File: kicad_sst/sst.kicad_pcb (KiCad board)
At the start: 2 copper layers, 75 x 75 mm, 35 parts

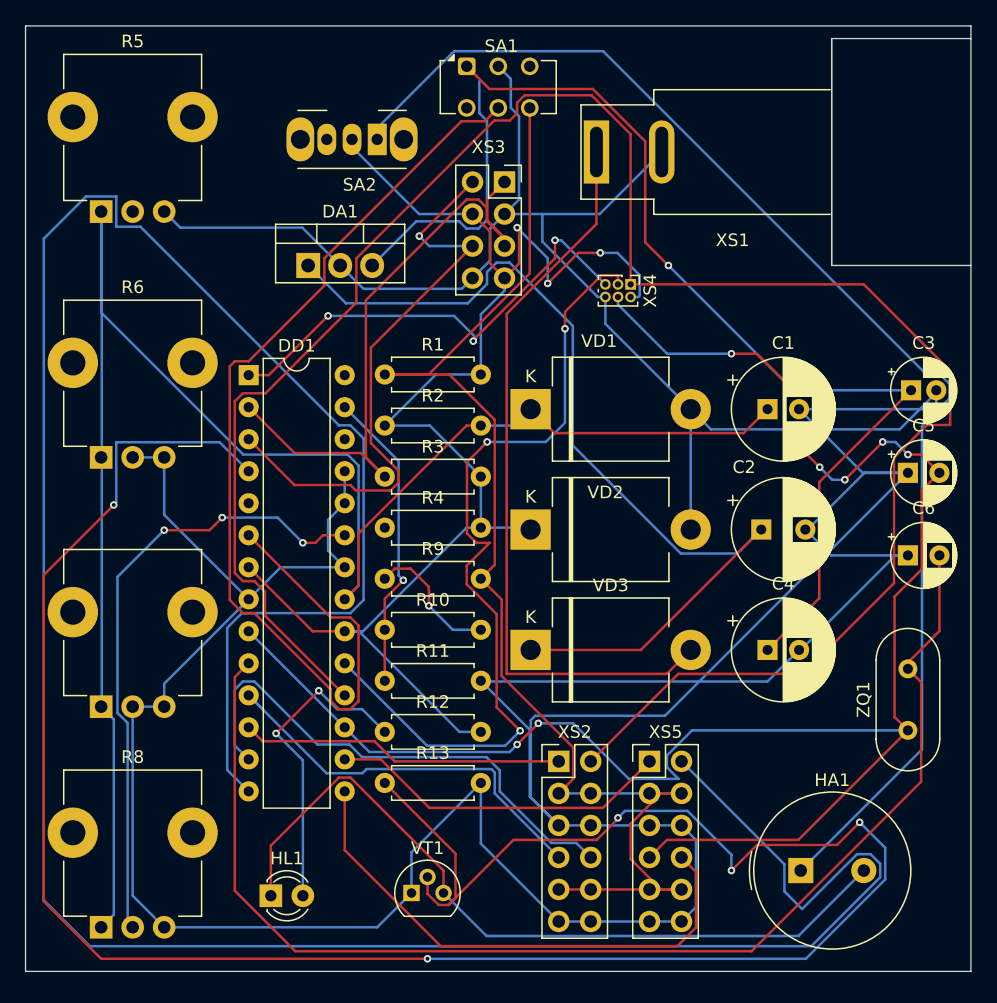
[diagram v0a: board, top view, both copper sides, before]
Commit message: version of PCB layout without errors
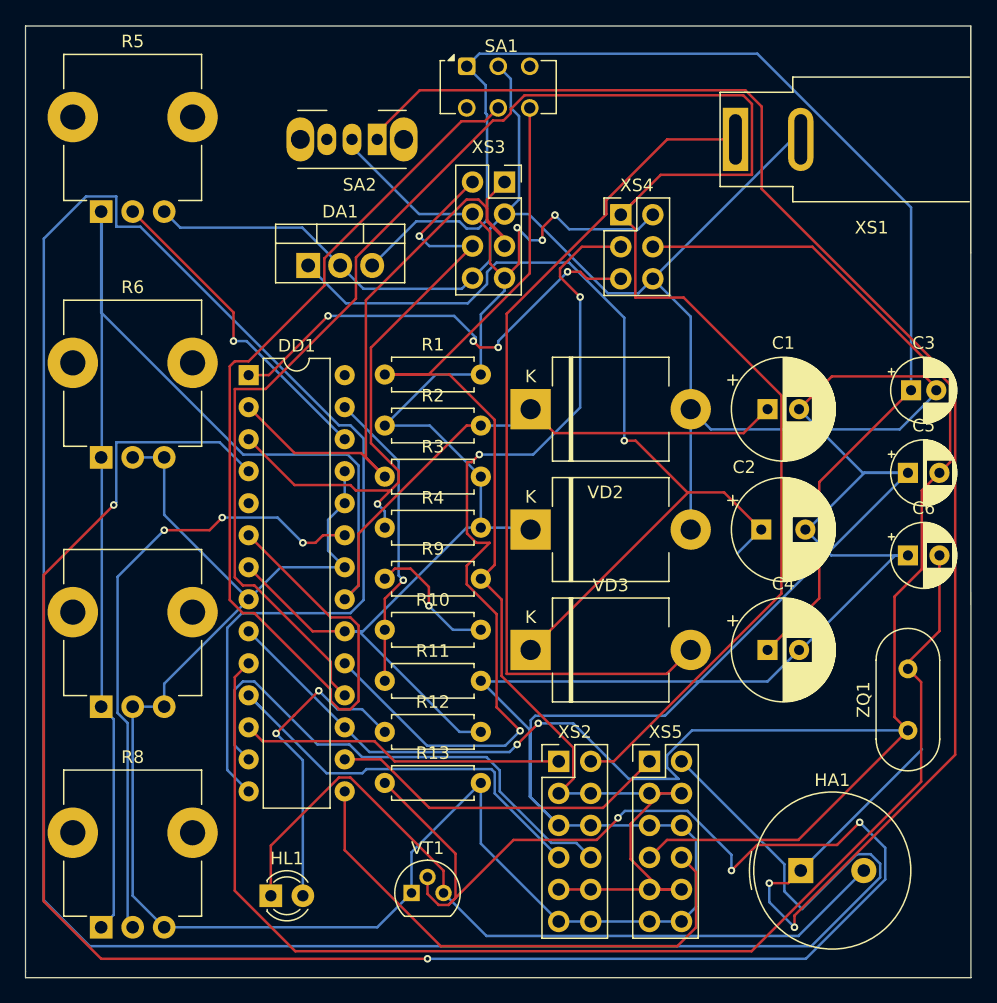
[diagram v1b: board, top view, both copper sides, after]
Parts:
- XS4: footprint Connector_PinHeader_1.00mm:PinHeader_2x03_P1.00mm_Vertical -> Connector_PinHeader_2.54mm:PinHeader_2x03_P2.54mm_Vertical
- moved XS1 11.1 mm to (131.3, 50.0)
- moved XS4 5.58 mm to (122.2, 56.0), turned to 0 degrees
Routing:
- net Net-(HA1-+): track 103.3 -> 131.4 mm, vias 0 -> 2
- net Net-(DD1-PC3): track 0.00 -> 25.6 mm, vias 0 -> 1
- net Net-(VD3-A): track 59.7 -> 68.5 mm
- net GND: track 395.3 -> 402.4 mm
- net Net-(DA1-OUT): track 99.8 -> 104.5 mm, vias 1 -> 0
- net Net-(DD1-EPB5): track 66.2 -> 70.3 mm
- net Net-(DD1-PB4): track 162.5 -> 158.7 mm
- net Net-(DD1-PD1): track 47.4 -> 51.1 mm, vias 1 -> 2
- net Net-(DA1-IN): track 77.2 -> 73.9 mm, vias 0 -> 1
- net +5V: track 113.2 -> 109.9 mm
- net Net-(DD1-~{RESET}/PC6): track 37.3 -> 36.2 mm, vias 3 -> 4
- net Net-(DD1-PB3): track 146.5 -> 145.5 mm, vias 7 -> 2
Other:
- board size 75 x 75 mm -> 75 x 75.5 mm

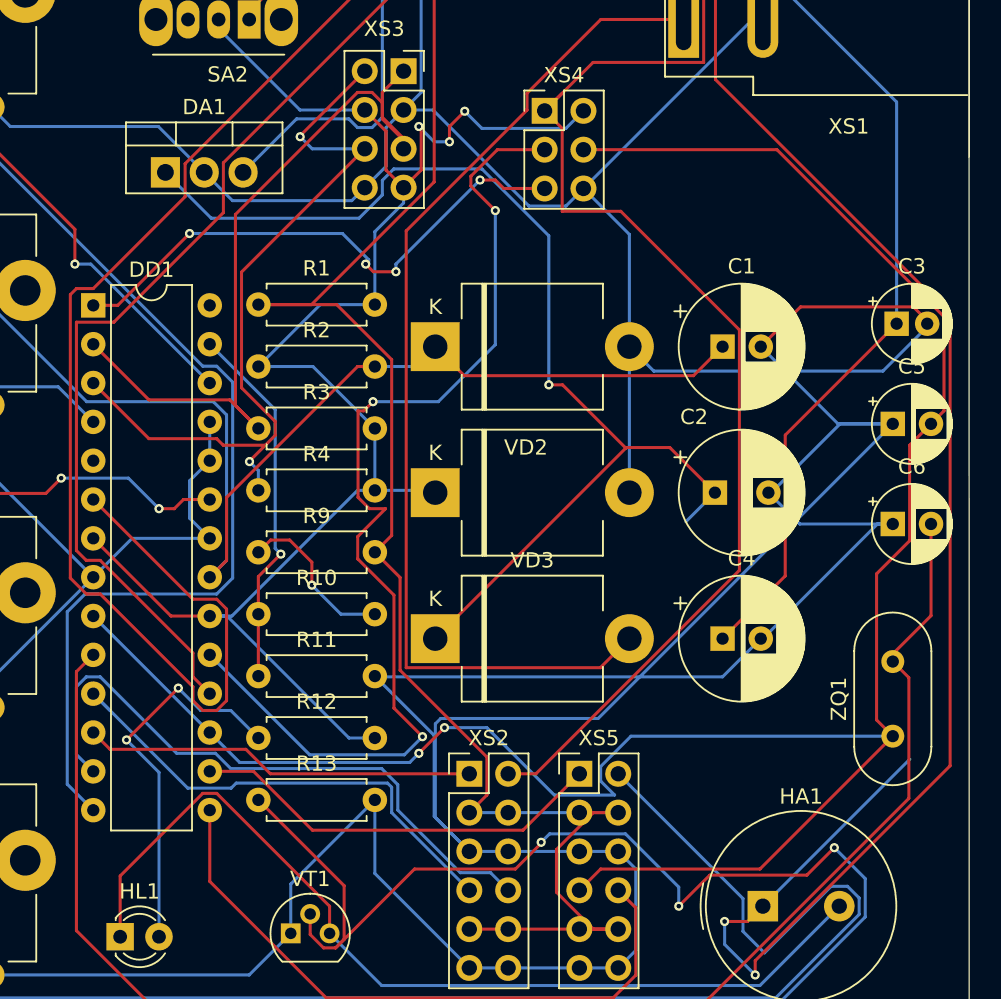
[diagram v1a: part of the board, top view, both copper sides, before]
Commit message: pcb without warnings
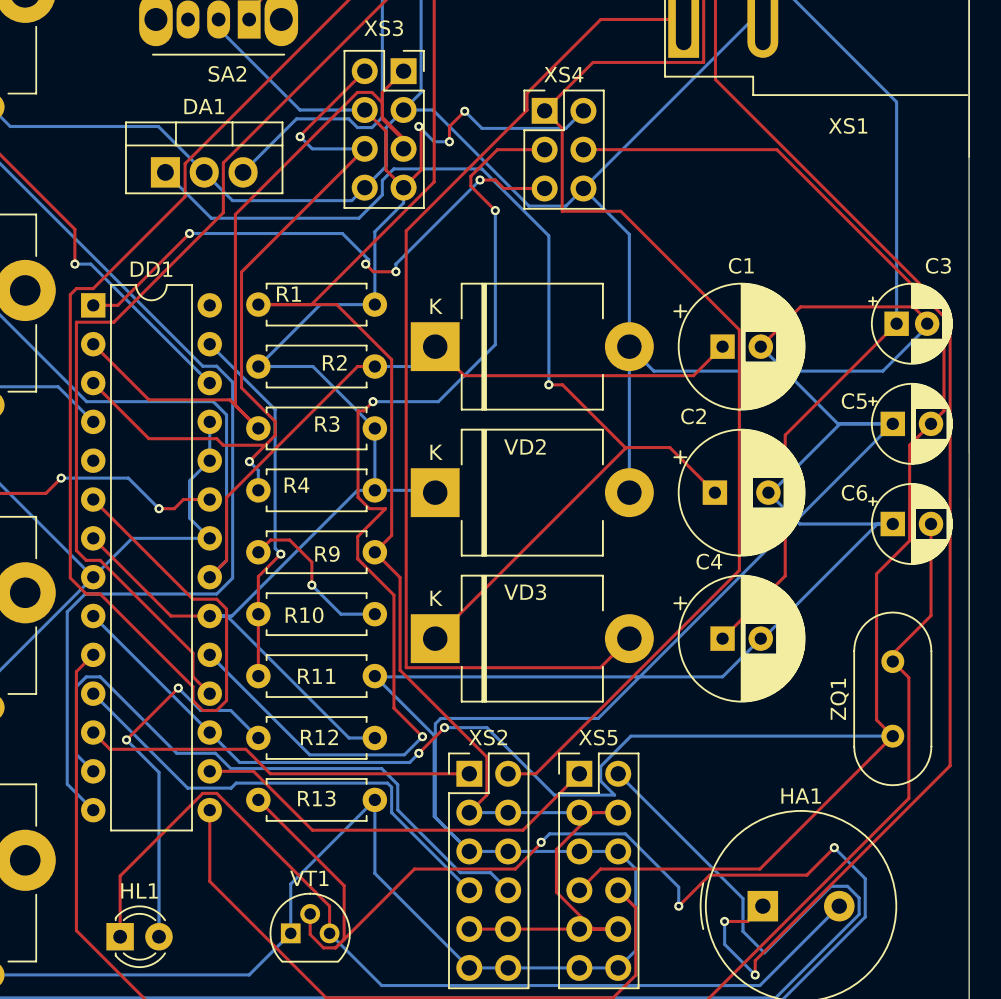
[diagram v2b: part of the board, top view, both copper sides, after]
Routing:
- net Net-(HA1-+): track 131.4 -> 117.8 mm
- net Net-(DA1-IN): track 73.9 -> 71.2 mm
- net Net-(DD1-PB4): track 158.7 -> 157.1 mm
- net Net-(DD1-PD5): track 32.7 -> 31.2 mm
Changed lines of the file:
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@@
 		(tags "CP Radial series Radial pin pitch 2.50mm  diameter 8mm Electrolytic Capacitor")
 		(property "Reference" "C4"
-			(at 1.25 -5.25 0)
+			(at -0.864923 -5 0)
 			(layer "F.SilkS")
 			(effects
@@
 		(tags "Resistor Axial_DIN0207 series Axial Horizontal pin pitch 7.62mm 0.25W = 1/4W length 6.3mm diameter 2.5mm")
 		(property "Reference" "R2"
-			(at 3.81 -2.37 0)
+			(at 4.999775 -0.2 0)
 			(layer "F.SilkS")
 			(effects
@@
 		(tags "CP Radial series Radial pin pitch 2.50mm  diameter 5mm Electrolytic Capacitor")
 		(property "Reference" "C5"
-			(at 1.25 -3.75 0)
+			(at -2.5 -1.45 0)
 			(layer "F.SilkS")
 			(effects
@@
 		(tags "Resistor Axial_DIN0207 series Axial Horizontal pin pitch 7.62mm 0.25W = 1/4W length 6.3mm diameter 2.5mm")
 		(property "Reference" "R4"
-			(at 3.81 -2.37 0)
+			(at 2.499775 -0.3 0)
 			(layer "F.SilkS")
 			(effects
@@
 		(tags "Resistor Axial_DIN0207 series Axial Horizontal pin pitch 7.62mm 0.25W = 1/4W length 6.3mm diameter 2.5mm")
 		(property "Reference" "R13"
-			(at 3.81 -2.37 0)
+			(at 3.81 -0.05 0)
 			(layer "F.SilkS")
 			(effects
@@
 		(tags "Resistor Axial_DIN0207 series Axial Horizontal pin pitch 7.62mm 0.25W = 1/4W length 6.3mm diameter 2.5mm")
 		(property "Reference" "R11"
-			(at 3.81 -2.37 0)
+			(at 3.81 0.05 0)
 			(layer "F.SilkS")
 			(effects
@@
 		(tags "Resistor Axial_DIN0207 series Axial Horizontal pin pitch 7.62mm 0.25W = 1/4W length 6.3mm diameter 2.5mm")
 		(property "Reference" "R9"
-			(at 3.81 -2.37 0)
+			(at 4.499775 0.15 0)
 			(layer "F.SilkS")
 			(effects
@@
 		(tags "CP Radial series Radial pin pitch 2.50mm  diameter 5mm Electrolytic Capacitor")
 		(property "Reference" "C6"
-			(at 1.25 -3.75 0)
+			(at -2.5 -2 0)
 			(layer "F.SilkS")
 			(effects
@@
 		(tags "Resistor Axial_DIN0207 series Axial Horizontal pin pitch 7.62mm 0.25W = 1/4W length 6.3mm diameter 2.5mm")
 		(property "Reference" "R12"
-			(at 3.81 -2.37 0)
+			(at 3.999775 0 0)
 			(layer "F.SilkS")
 			(effects
@@
 		(tags "CP Radial series Radial pin pitch 2.00mm  diameter 5mm Electrolytic Capacitor")
 		(property "Reference" "C3"
-			(at 1 -3.75 0)
+			(at 2.75 -3.75 0)
 			(layer "F.SilkS")
 			(effects
@@
 		(tags "Resistor Axial_DIN0207 series Axial Horizontal pin pitch 7.62mm 0.25W = 1/4W length 6.3mm diameter 2.5mm")
 		(property "Reference" "R10"
-			(at 3.81 -2.37 0)
+			(at 2.999775 0.1 0)
 			(layer "F.SilkS")
 			(effects
@@
 		(tags "Resistor Axial_DIN0207 series Axial Horizontal pin pitch 7.62mm 0.25W = 1/4W length 6.3mm diameter 2.5mm")
 		(property "Reference" "R1"
-			(at 3.81 -2.37 0)
+			(at 1.999775 -0.65 0)
 			(layer "F.SilkS")
 			(effects
@@
 		(tags "Diode 5KPW series Axial Horizontal pin pitch 12.7mm  length 9mm diameter 8mm")
 		(property "Reference" "VD3"
-			(at 6.35 -5.12 0)
+			(at 5.929775 -3 0)
 			(layer "F.SilkS")
 			(effects
@@
 		(tags "Resistor Axial_DIN0207 series Axial Horizontal pin pitch 7.62mm 0.25W = 1/4W length 6.3mm diameter 2.5mm")
 		(property "Reference" "R3"
-			(at 3.81 -2.37 0)
+			(at 4.499775 -0.25 0)
 			(layer "F.SilkS")
 			(effects
@@
 	)
 	(segment
-		(start 133.364923 80.95)
-		(end 131.464923 82.85)
-		(width 0.2)
-		(layer "B.Cu")
-		(net 3)
-	)
-	(segment
 		(start 111.61 61.476346)
 		(end 110.086346 63)
@@
 	)
 	(segment
-		(start 123.375 54.825)
+		(start 125.39 52.81)
 		(end 122.225 55.975)
 		(width 0.2)
@@
 	)
 	(segment
-		(start 122.225 55.975)
-		(end 123.375 57.125)
+		(start 113.5 47.585786)
+		(end 114.585786 46.5)
 		(width 0.2)
 		(layer "F.Cu")
@@
 	)
 	(segment
-		(start 92.24459 85.38)
-		(end 91.600225 84.735635)
+		(start 122.225 55.975)
+		(end 123.375 57.125)
 		(width 0.2)
 		(layer "F.Cu")
@@
 	)
 	(segment
-		(start 101.2125 62.636029)
-		(end 101.2125 59.373286)
+		(start 91.600225 69.8)
+		(end 94.048529 69.8)
 		(width 0.2)
 		(layer "F.Cu")
@@
 	)
 	(segment
-		(start 101.2125 59.373286)
-		(end 112.085786 48.5)
+		(start 99.220225 91.444365)
+		(end 93.15586 85.38)
 		(width 0.2)
 		(layer "F.Cu")
@@
 	)
 	(segment
-		(start 131.94 46.5)
-		(end 132.63 47.19)
-		(width 0.2)
-		(layer "F.Cu")
-		(net 9)
-	)
-	(segment
 		(start 112.914214 48.5)
 		(end 113.5 47.914214)
@@
 	)
 	(segment
-		(start 113.5 47.914214)
-		(end 113.5 47.585786)
+		(start 134.964923 70.3)
+		(end 134.964923 86.035077)
 		(width 0.2)
 		(layer "F.Cu")
@@
 	)
 	(segment
-		(start 134.964923 70.3)
-		(end 134.964923 86.035077)
+		(start 112.085786 48.5)
+		(end 112.914214 48.5)
 		(width 0.2)
 		(layer "F.Cu")
@@
 	)
 	(segment
-		(start 114.585786 46.5)
-		(end 131.94 46.5)
+		(start 93.15586 85.38)
+		(end 92.24459 85.38)
 		(width 0.2)
 		(layer "F.Cu")
@@
 	)
 	(segment
-		(start 99.220225 91.444365)
-		(end 93.15586 85.38)
+		(start 91.600225 84.735635)
+		(end 91.600225 69.8)
 		(width 0.2)
 		(layer "F.Cu")
@@
 	)
 	(segment
-		(start 93.15586 85.38)
-		(end 92.24459 85.38)
+		(start 131.94 46.5)
+		(end 132.63 47.19)
 		(width 0.2)
 		(layer "F.Cu")
@@
 	)
 	(segment
-		(start 132.63 52.81)
-		(end 125.39 52.81)
+		(start 114.585786 46.5)
+		(end 131.94 46.5)
 		(width 0.2)
 		(layer "F.Cu")
@@
 	)
 	(segment
-		(start 123.375 62.544391)
-		(end 127.209314 62.544391)
+		(start 92.24459 85.38)
+		(end 91.600225 84.735635)
 		(width 0.2)
 		(layer "F.Cu")
@@
 	)
 	(segment
-		(start 121.66 99.34)
-		(end 119.84 99.34)
+		(start 123.375 62.544391)
+		(end 127.209314 62.544391)
 		(width 0.2)
 		(layer "F.Cu")
@@
 	)
 	(segment
-		(start 125.39 52.81)
-		(end 122.225 55.975)
+		(start 121.66 99.34)
+		(end 119.84 99.34)
 		(width 0.2)
 		(layer "F.Cu")
@@
 	)
 	(segment
-		(start 99.220225 93)
-		(end 99.220225 91.444365)
+		(start 113.5 47.914214)
+		(end 113.5 47.585786)
 		(width 0.2)
 		(layer "F.Cu")
@@
 	)
 	(segment
-		(start 91.600225 69.8)
-		(end 94.048529 69.8)
+		(start 132.63 52.81)
+		(end 125.39 52.81)
 		(width 0.2)
 		(layer "F.Cu")
@@
 	)
 	(segment
-		(start 112.085786 48.5)
-		(end 112.914214 48.5)
+		(start 101.2125 62.636029)
+		(end 101.2125 59.373286)
 		(width 0.2)
 		(layer "F.Cu")
@@
 	)
 	(segment
-		(start 100.320225 94.1)
-		(end 99.220225 93)
+		(start 127.209314 62.544391)
+		(end 134.964923 70.3)
 		(width 0.2)
 		(layer "F.Cu")
@@
 	)
 	(segment
-		(start 91.600225 84.735635)
-		(end 91.600225 69.8)
+		(start 134.964923 86.035077)
+		(end 121.66 99.34)
 		(width 0.2)
 		(layer "F.Cu")
@@
 	)
 	(segment
-		(start 127.209314 62.544391)
-		(end 134.964923 70.3)
+		(start 99.220225 93)
+		(end 99.220225 91.444365)
 		(width 0.2)
 		(layer "F.Cu")
@@
 	)
 	(segment
-		(start 134.964923 86.035077)
-		(end 121.66 99.34)
+		(start 132.63 47.19)
+		(end 132.63 52.81)
 		(width 0.2)
 		(layer "F.Cu")
@@
 	)
 	(segment
-		(start 132.63 47.19)
-		(end 132.63 52.81)
+		(start 100.320225 94.1)
+		(end 99.220225 93)
 		(width 0.2)
 		(layer "F.Cu")
@@
 	)
 	(segment
-		(start 113.5 47.585786)
-		(end 114.585786 46.5)
+		(start 101.2125 59.373286)
+		(end 112.085786 48.5)
 		(width 0.2)
 		(layer "F.Cu")
@@
 	)
 	(segment
-		(start 92.700225 94.1)
-		(end 93.800225 95.2)
-		(width 0.2)
-		(layer "B.Cu")
-		(net 22)
-	)
-	(segment
 		(start 98.880225 100.28)
 		(end 92.700225 94.1)
@@
 		(net 27)
 	)
-	(segment
-		(start 146.115686 98.384314)
-		(end 136.5 108)
-		(width 0.2)
-		(layer "B.Cu")
-		(net 27)
-	)

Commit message: deleted all tracks
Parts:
- removed R13: R, Resistor_THT:R_Axial_DIN0207_L6.3mm_D2.5mm_P7.62mm_Horizontal
- moved R8 133.5 mm to (213.0, 132.7)
- moved DD1 129.2 mm to (221.9, 70.2)
- moved XS3 126.0 mm to (237.8, 70.5)
- moved R7 120.1 mm to (195.0, 132.7)
- moved XS4 116.4 mm to (235.2, 84.0)
- moved R4 113.0 mm to (216.5, 81.8), turned to 90 degrees
- moved R6 111.9 mm to (177.0, 132.7)
- moved XS5 111.3 mm to (235.7, 96.7)
- moved R5 110.0 mm to (159.5, 132.7)
- moved VD1 109.6 mm to (224.2, 61.0)
- moved XS2 96.8 mm to (213.5, 88.5)
- moved HL1 91.0 mm to (131.7, 27.0)
- moved R12 85.4 mm to (169.7, 43.0)
- moved VT1 84.4 mm to (124.5, 27.5)
- moved ZQ1 84.1 mm to (227.9, 110.5), turned to 180 degrees
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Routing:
- net GND: track 402.4 -> 0.00 mm
- net Net-(DD1-PB0): track 222.0 -> 0.00 mm
- net Net-(DD1-PD2): track 182.5 -> 0.00 mm, vias 5 -> 0
- net Net-(DD1-PB4): track 157.1 -> 0.00 mm
- net +2V5: track 146.0 -> 0.00 mm
- net Net-(DD1-PB3): track 145.5 -> 0.00 mm, vias 2 -> 0
- net Net-(HA1-+): track 117.8 -> 0.00 mm, vias 2 -> 0
- net +5V: track 109.9 -> 0.00 mm, vias 3 -> 0
- net Net-(DA1-OUT): track 104.5 -> 0.00 mm
- net +BATT: track 104.1 -> 0.00 mm
- net Net-(DD1-XTAL2/PB7): track 99.9 -> 0.00 mm
- net Net-(DD1-PD4): track 81.9 -> 0.00 mm
- net Net-(DA1-IN): track 71.2 -> 0.00 mm, vias 1 -> 0
- net Net-(DD1-EPB5): track 70.3 -> 0.00 mm, vias 3 -> 0
- net Net-(VD3-A): track 68.5 -> 0.00 mm
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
